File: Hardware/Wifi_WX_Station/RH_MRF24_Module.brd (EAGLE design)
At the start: 23.8 x 33.6 mm, 7 parts, among them M1 MRF24WB0MA

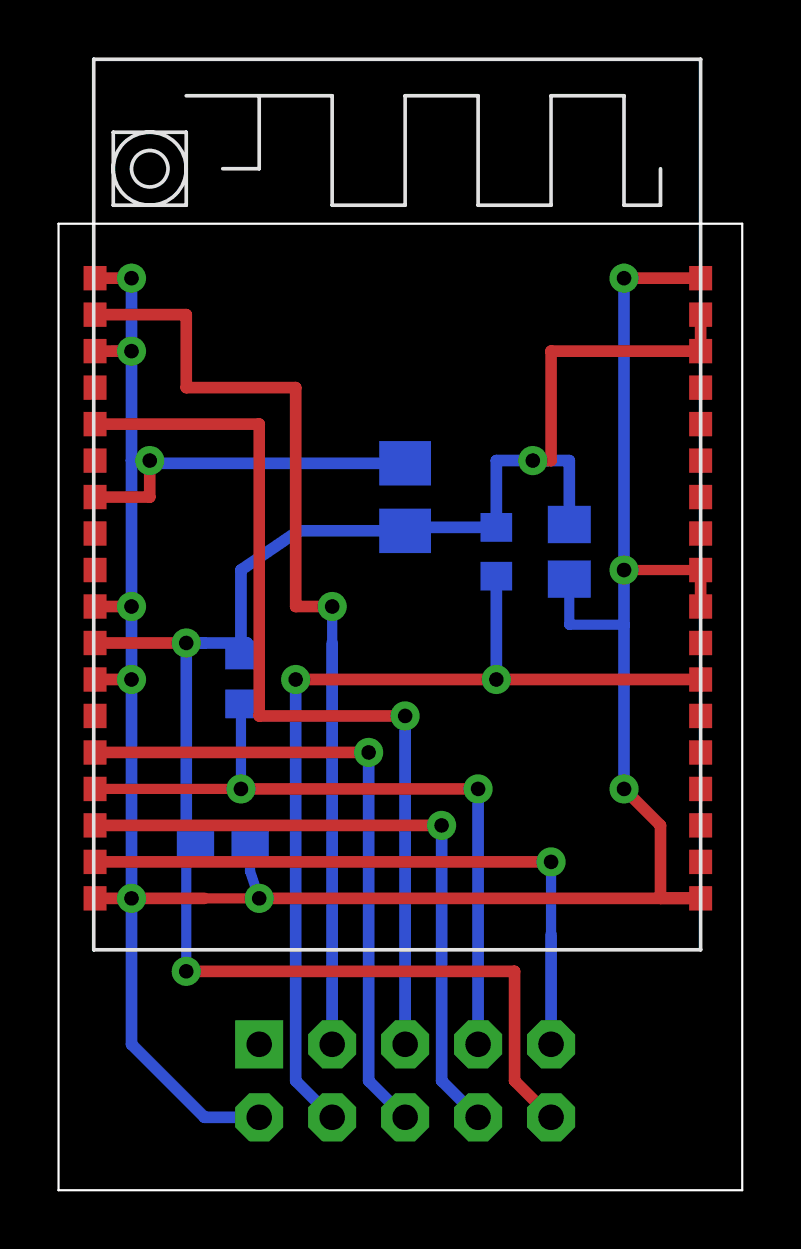
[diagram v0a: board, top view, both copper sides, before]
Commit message: Modified the RF carrier slightly with longer pads for easier soldering.
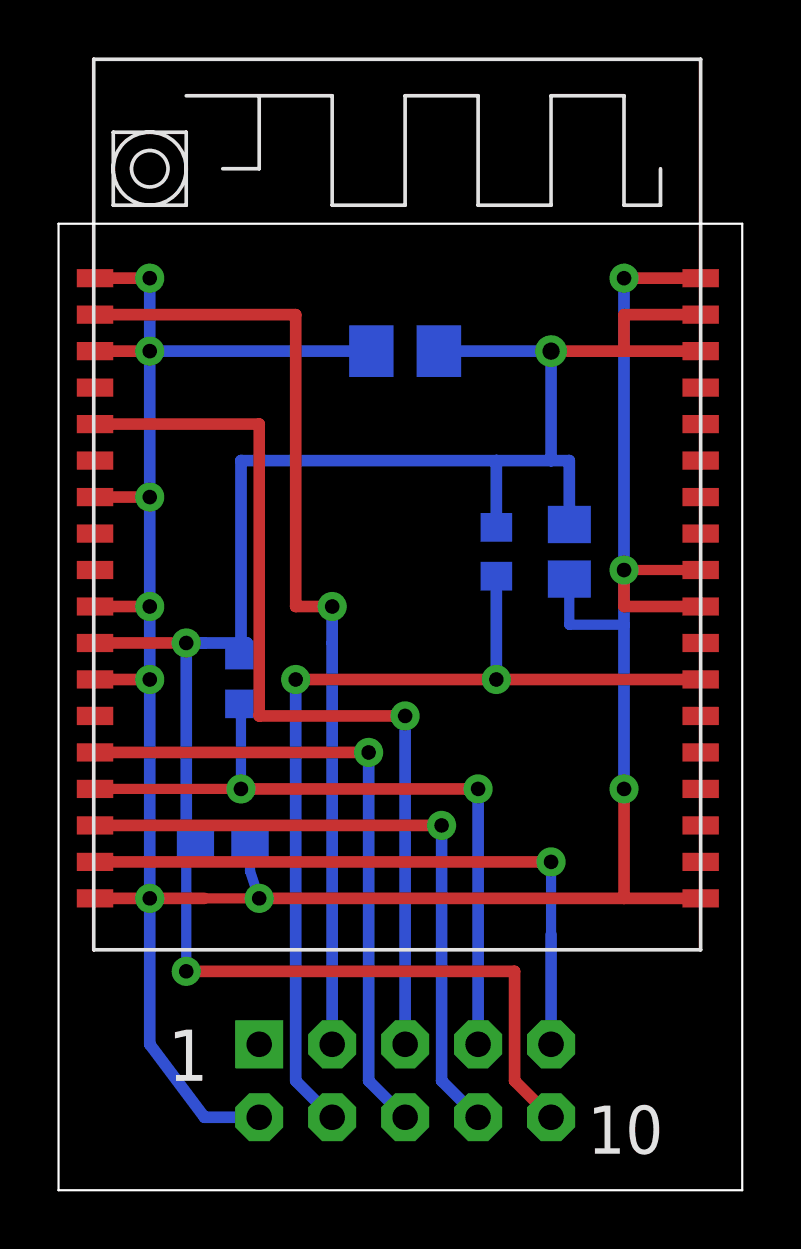
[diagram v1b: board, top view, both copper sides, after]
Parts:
- moved C3 5.08 mm to (14.0, 30.5), turned to 180 degrees
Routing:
- net +3V3: track 65.6 -> 74.8 mm
- net GND: track 107.3 -> 106.4 mm
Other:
- board text added: "1"
- board text added: "10"
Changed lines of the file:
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@@
 <?xml version="1.0" encoding="utf-8"?>
 <!DOCTYPE eagle SYSTEM "eagle.dtd">
-<eagle version="6.3">
+<eagle version="6.5.0">
 <drawing>
 <settings>
@@
 <text x="24.13" y="33.02" size="1.4224" layer="26" font="vector" rot="MR270">RV Builders Product 2013</text>
 <text x="3.81" y="29.21" size="1.4224" layer="26" font="vector" rot="MR270">Wifi WX-Station</text>
+<text x="5.715" y="5.08" size="1.778" layer="21">1</text>
+<text x="20.32" y="2.54" size="1.6764" layer="21">10</text>
 </plain>
 <attributes>
@@
 <attribute name="NAME" x="6.985" y="17.78" size="1.27" layer="26" rot="MR270"/>
 </element>
-<element name="C3" library="rcl" package="R/2012-12R" value="4.7uF" x="13.97" y="25.4" smashed="yes" rot="MR270">
-<attribute name="NAME" x="11.7" y="24.175" size="1.27" layer="26" rot="MR270"/>
+<element name="C3" library="rcl" package="R/2012-12R" value="4.7uF" x="13.97" y="30.48" smashed="yes" rot="MR180">
+<attribute name="NAME" x="12.655" y="29.48" size="1.27" layer="26" rot="MR180"/>
 </element>
 <element name="JP1" library="wifi_WX" package="2X5-RA-HEADER" value="M05X2" x="13.97" y="5.08" smashed="yes" rot="MR270"/>
@@
 <contactref element="JP1" pad="2"/>
 <contactref element="M1" pad="21"/>
-<wire x1="6.985" y1="11.43" x2="4.445" y2="11.43" width="0.4064" layer="1"/>
-<wire x1="24.257" y1="22.86" x2="24.257" y2="21.59" width="0.4064" layer="1"/>
+<wire x1="6.985" y1="11.43" x2="5.08" y2="11.43" width="0.4064" layer="1"/>
 <wire x1="3.175" y1="25.4" x2="5.08" y2="25.4" width="0.4064" layer="1"/>
-<wire x1="5.08" y1="25.4" x2="5.08" y2="26.67" width="0.4064" layer="1"/>
-<via x="5.08" y="26.67" extent="1-16" drill="0.508"/>
+<via x="5.08" y="25.4" extent="1-16" drill="0.508"/>
 <wire x1="6.985" y1="11.43" x2="8.89" y2="11.43" width="0.3556" layer="1"/>
-<wire x1="8.89" y1="11.43" x2="24.257" y2="11.43" width="0.4064" layer="1"/>
+<wire x1="8.89" y1="11.43" x2="21.59" y2="11.43" width="0.4064" layer="1"/>
 <wire x1="24.257" y1="22.86" x2="21.59" y2="22.86" width="0.3556" layer="1"/>
 <via x="21.59" y="22.86" extent="1-16" drill="0.508"/>
@@
 <via x="21.59" y="33.02" extent="1-16" drill="0.508"/>
 <wire x1="21.59" y1="33.02" x2="21.59" y2="22.86" width="0.4064" layer="16"/>
-<wire x1="24.257" y1="11.43" x2="22.86" y2="11.43" width="0.4064" layer="1"/>
-<wire x1="22.86" y1="11.43" x2="22.86" y2="13.97" width="0.4064" layer="1"/>
-<wire x1="22.86" y1="13.97" x2="21.59" y2="15.24" width="0.4064" layer="1"/>
+<wire x1="24.257" y1="11.43" x2="21.59" y2="11.43" width="0.4064" layer="1"/>
+<wire x1="21.59" y1="11.43" x2="21.59" y2="15.24" width="0.4064" layer="1"/>
 <via x="21.59" y="15.24" extent="1-16" drill="0.508"/>
 <wire x1="21.59" y1="15.24" x2="21.59" y2="20.955" width="0.4064" layer="16"/>
 <wire x1="21.59" y1="20.955" x2="21.59" y2="22.86" width="0.4064" layer="16"/>
-<wire x1="3.175" y1="33.02" x2="4.445" y2="33.02" width="0.4064" layer="1"/>
-<via x="4.445" y="33.02" extent="1-16" drill="0.508"/>
-<wire x1="4.445" y1="33.02" x2="4.445" y2="30.48" width="0.4064" layer="16"/>
-<wire x1="4.445" y1="30.48" x2="3.81" y2="30.48" width="0.4064" layer="16"/>
-<wire x1="4.445" y1="30.48" x2="4.445" y2="26.67" width="0.4064" layer="16"/>
-<wire x1="4.445" y1="26.67" x2="5.08" y2="26.67" width="0.4064" layer="16"/>
-<wire x1="3.175" y1="21.59" x2="4.445" y2="21.59" width="0.4064" layer="1"/>
-<via x="4.445" y="21.59" extent="1-16" drill="0.508"/>
-<wire x1="4.445" y1="21.59" x2="4.445" y2="26.67" width="0.4064" layer="16"/>
-<via x="4.445" y="19.05" extent="1-16" drill="0.508"/>
-<wire x1="4.445" y1="19.05" x2="4.445" y2="21.59" width="0.4064" layer="16"/>
-<wire x1="3.175" y1="30.48" x2="4.445" y2="30.48" width="0.4064" layer="1"/>
-<via x="4.445" y="30.48" extent="1-16" drill="0.508"/>
-<wire x1="3.175" y1="19.05" x2="4.445" y2="19.05" width="0.4064" layer="1"/>
-<wire x1="4.445" y1="19.05" x2="4.445" y2="11.43" width="0.4064" layer="16"/>
-<via x="4.445" y="11.43" extent="1-16" drill="0.508"/>
-<wire x1="4.445" y1="11.43" x2="3.175" y2="11.43" width="0.4064" layer="1"/>
-<wire x1="5.08" y1="26.67" x2="5.175" y2="26.575" width="0.4064" layer="16"/>
-<wire x1="5.175" y1="26.575" x2="13.97" y2="26.575" width="0.4064" layer="16"/>
+<wire x1="3.175" y1="33.02" x2="5.08" y2="33.02" width="0.4064" layer="1"/>
+<via x="5.08" y="33.02" extent="1-16" drill="0.508"/>
+<wire x1="5.08" y1="33.02" x2="5.08" y2="30.48" width="0.4064" layer="16"/>
+<wire x1="5.08" y1="30.48" x2="5.08" y2="25.4" width="0.4064" layer="16"/>
+<wire x1="3.175" y1="21.59" x2="5.08" y2="21.59" width="0.4064" layer="1"/>
+<via x="5.08" y="21.59" extent="1-16" drill="0.508"/>
+<wire x1="5.08" y1="21.59" x2="5.08" y2="25.4" width="0.4064" layer="16"/>
+<via x="5.08" y="19.05" extent="1-16" drill="0.508"/>
+<wire x1="5.08" y1="19.05" x2="5.08" y2="21.59" width="0.4064" layer="16"/>
+<wire x1="3.175" y1="30.48" x2="5.08" y2="30.48" width="0.4064" layer="1"/>
+<via x="5.08" y="30.48" extent="1-16" drill="0.508"/>
+<wire x1="3.175" y1="19.05" x2="5.08" y2="19.05" width="0.4064" layer="1"/>
+<wire x1="5.08" y1="19.05" x2="5.08" y2="11.43" width="0.4064" layer="16"/>
+<via x="5.08" y="11.43" extent="1-16" drill="0.508"/>
+<wire x1="5.08" y1="11.43" x2="3.175" y2="11.43" width="0.4064" layer="1"/>
 <wire x1="8.89" y1="3.81" x2="6.985" y2="3.81" width="0.4064" layer="16"/>
-<wire x1="6.985" y1="3.81" x2="4.445" y2="6.35" width="0.4064" layer="16"/>
-<wire x1="4.445" y1="6.35" x2="4.445" y2="11.43" width="0.4064" layer="16"/>
+<wire x1="6.985" y1="3.81" x2="5.08" y2="6.35" width="0.4064" layer="16"/>
+<wire x1="5.08" y1="6.35" x2="5.08" y2="11.43" width="0.4064" layer="16"/>
+<wire x1="5.08" y1="30.48" x2="12.795" y2="30.48" width="0.4064" layer="16"/>
+<wire x1="24.257" y1="21.59" x2="21.59" y2="21.59" width="0.4064" layer="1"/>
+<wire x1="21.59" y1="21.59" x2="21.59" y2="22.86" width="0.4064" layer="1"/>
 </signal>
 <signal name="+3V3">
@@
 <wire x1="6.35" y1="20.32" x2="6.985" y2="20.32" width="0.4064" layer="16"/>
 <wire x1="6.35" y1="13.335" x2="6.35" y2="20.32" width="0.4064" layer="16"/>
-<wire x1="18.415" y1="26.67" x2="19.05" y2="26.67" width="0.4064" layer="1"/>
-<wire x1="19.05" y1="26.67" x2="19.05" y2="30.48" width="0.4064" layer="1"/>
-<wire x1="19.05" y1="30.48" x2="24.257" y2="30.48" width="0.4064" layer="1"/>
-<wire x1="24.257" y1="30.48" x2="24.257" y2="31.75" width="0.4064" layer="1"/>
-<via x="18.415" y="26.67" extent="1-16" drill="0.508"/>
+<wire x1="21.59" y1="30.48" x2="24.257" y2="30.48" width="0.4064" layer="1"/>
 <wire x1="17.78" y1="8.89" x2="6.35" y2="8.89" width="0.4064" layer="1"/>
 <via x="6.35" y="8.89" extent="1-16" drill="0.508"/>
@@
 <wire x1="8.255" y1="19.9" x2="8.47" y2="20.32" width="0.4064" layer="16"/>
 <wire x1="8.47" y1="20.32" x2="6.35" y2="20.32" width="0.4064" layer="16"/>
-<wire x1="17.145" y1="24.345" x2="13.97" y2="24.345" width="0.4064" layer="16"/>
-<wire x1="13.97" y1="24.345" x2="13.97" y2="24.225" width="0.4064" layer="16"/>
-<wire x1="8.255" y1="19.9" x2="8.255" y2="22.86" width="0.4064" layer="16"/>
-<wire x1="8.255" y1="22.86" x2="10.255" y2="24.225" width="0.4064" layer="16"/>
-<wire x1="10.255" y1="24.225" x2="13.97" y2="24.225" width="0.4064" layer="16"/>
 <wire x1="17.145" y1="24.345" x2="17.145" y2="26.67" width="0.4064" layer="16"/>
-<wire x1="17.145" y1="26.67" x2="18.415" y2="26.67" width="0.4064" layer="16"/>
 <wire x1="19.685" y1="24.445" x2="19.685" y2="26.67" width="0.4064" layer="16"/>
-<wire x1="19.685" y1="26.67" x2="18.415" y2="26.67" width="0.4064" layer="16"/>
+<wire x1="19.685" y1="26.67" x2="19.05" y2="26.67" width="0.4064" layer="16"/>
+<wire x1="19.05" y1="26.67" x2="17.145" y2="26.67" width="0.4064" layer="16"/>
 <wire x1="17.78" y1="8.89" x2="17.78" y2="5.08" width="0.4064" layer="1"/>
 <wire x1="17.78" y1="5.08" x2="19.05" y2="3.81" width="0.4064" layer="1"/>
 <wire x1="6.67" y1="13.335" x2="6.35" y2="13.335" width="0.4064" layer="16"/>
+<wire x1="8.255" y1="19.9" x2="8.255" y2="26.67" width="0.4064" layer="16"/>
+<wire x1="8.255" y1="26.67" x2="17.145" y2="26.67" width="0.4064" layer="16"/>
+<wire x1="24.257" y1="31.75" x2="21.59" y2="31.75" width="0.4064" layer="1"/>
+<wire x1="21.59" y1="31.75" x2="21.59" y2="30.48" width="0.4064" layer="1"/>
+<wire x1="15.145" y1="30.48" x2="19.05" y2="30.48" width="0.4064" layer="16"/>
+<via x="19.05" y="30.48" extent="1-16" drill="0.6"/>
+<wire x1="19.05" y1="30.48" x2="21.59" y2="30.48" width="0.4064" layer="1"/>
+<wire x1="19.05" y1="30.48" x2="19.05" y2="26.67" width="0.4064" layer="16"/>
 </signal>
 <signal name="HIBER">
 <contactref element="M1" pad="20"/>
-<wire x1="10.16" y1="21.59" x2="10.16" y2="29.21" width="0.4064" layer="1"/>
-<wire x1="10.16" y1="29.21" x2="6.35" y2="29.21" width="0.4064" layer="1"/>
-<wire x1="6.35" y1="29.21" x2="6.35" y2="31.75" width="0.4064" layer="1"/>
-<wire x1="6.35" y1="31.75" x2="3.175" y2="31.75" width="0.4064" layer="1"/>
+<wire x1="10.16" y1="21.59" x2="10.16" y2="31.75" width="0.4064" layer="1"/>
+<wire x1="10.16" y1="31.75" x2="3.175" y2="31.75" width="0.4064" layer="1"/>
 <contactref element="JP1" pad="3"/>
 <wire x1="10.16" y1="21.59" x2="11.43" y2="21.59" width="0.4064" layer="1"/>
 <via x="11.43" y="21.59" extent="1-16" drill="0.508"/>
-<wire x1="11.43" y1="21.59" x2="11.43" y2="20.32" width="0.3556" layer="16"/>
+<wire x1="11.43" y1="21.59" x2="11.43" y2="20.32" width="0.4064" layer="16"/>
 <wire x1="11.43" y1="20.32" x2="11.43" y2="6.35" width="0.4064" layer="16"/>
 </signal>
